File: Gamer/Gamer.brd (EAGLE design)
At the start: 168.9 x 63.5 mm, 44 parts, among them J1 HEADER-1X8, J2 HEADER-1X8, J3 HEADER-1X8, J4 HEADER-1X8, J5 HEADER-1X8, J6 HEADER-1X8, J7 HEADER-1X8, J8 HEADER-1X8, U1 MMA8653FCR1, U2 ATTINY48, U3 ULN2803AFWG, U4 ATTINY48, U5 ULN2803AFWG, U6 ATTINY48, U7 ULN2803AFWG, U8 ATTINY48, U9 ULN2803AFWG

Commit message: gamer - properly chained MISO/MOSI through LED matrices
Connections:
- new net 10/MISO: PROG4.4, U8.PB3
- new net MOSI2/MISO3: PROG2.4, PROG3.1, U4.PB3, U6.PB4
- new net MOSI3/MISO4: PROG3.4, PROG4.1, U6.PB3, U8.PB4
- net 9/MISO: no longer PROG2.1, PROG3.1, PROG4.1, U4.PB4, U6.PB4, U8.PB4
- net MOSI1/MISO2: now also PROG2.1, U4.PB4; no longer PROG2.4, PROG3.4, PROG4.4, U4.PB3, U6.PB3, U8.PB3
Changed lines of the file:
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@@
 <contactref element="P1" pad="21"/>
 <contactref element="U2" pad="PB4"/>
-<contactref element="U4" pad="PB4"/>
-<contactref element="U6" pad="PB4"/>
-<contactref element="U8" pad="PB4"/>
 <contactref element="PROG1" pad="1"/>
-<contactref element="PROG2" pad="1"/>
-<contactref element="PROG3" pad="1"/>
-<contactref element="PROG4" pad="1"/>
-<wire x1="133.35" y1="60.96" x2="143.51" y2="60.96" width="0" layer="19" extent="1-1"/>
-<wire x1="123.19" y1="60.96" x2="133.35" y2="60.96" width="0" layer="19" extent="1-1"/>
-<wire x1="113.03" y1="60.96" x2="123.19" y2="60.96" width="0" layer="19" extent="1-1"/>
-<wire x1="135.89" y1="44.45" x2="133.35" y2="60.96" width="0" layer="19" extent="1-1"/>
-<wire x1="95.51" y1="44.01" x2="113.03" y2="60.96" width="0" layer="19" extent="1-1"/>
-<wire x1="63.76" y1="44.01" x2="95.51" y2="44.01" width="0" layer="19" extent="1-1"/>
-<wire x1="95.51" y1="12.26" x2="95.51" y2="44.01" width="0" layer="19" extent="1-1"/>
-<wire x1="63.76" y1="12.26" x2="63.76" y2="44.01" width="0" layer="19" extent="1-1"/>
+<wire x1="113.03" y1="60.96" x2="135.89" y2="44.45" width="0" layer="19" extent="1-1"/>
+<wire x1="63.76" y1="44.01" x2="113.03" y2="60.96" width="0" layer="19" extent="1-1"/>
 </signal>
 <signal name="11/SCLK">
@@
 <contactref element="U2" pad="PB3"/>
 <contactref element="PROG1" pad="4"/>
-<contactref element="U4" pad="PB3"/>
-<contactref element="PROG2" pad="4"/>
-<contactref element="U6" pad="PB3"/>
-<contactref element="PROG3" pad="4"/>
-<contactref element="U8" pad="PB3"/>
-<contactref element="PROG4" pad="4"/>
-<wire x1="135.89" y1="58.42" x2="146.05" y2="58.42" width="0" layer="19" extent="1-1"/>
-<wire x1="125.73" y1="58.42" x2="135.89" y2="58.42" width="0" layer="19" extent="1-1"/>
-<wire x1="115.57" y1="58.42" x2="125.73" y2="58.42" width="0" layer="19" extent="1-1"/>
-<wire x1="94.71" y1="44.01" x2="115.57" y2="58.42" width="0" layer="19" extent="1-1"/>
-<wire x1="62.96" y1="44.01" x2="94.71" y2="44.01" width="0" layer="19" extent="1-1"/>
-<wire x1="94.71" y1="12.26" x2="94.71" y2="44.01" width="0" layer="19" extent="1-1"/>
-<wire x1="62.96" y1="12.26" x2="62.96" y2="44.01" width="0" layer="19" extent="1-1"/>
+<contactref element="U4" pad="PB4"/>
+<contactref element="PROG2" pad="1"/>
+<wire x1="115.57" y1="58.42" x2="123.19" y2="60.96" width="0" layer="19" extent="1-1"/>
+<wire x1="95.51" y1="44.01" x2="115.57" y2="58.42" width="0" layer="19" extent="1-1"/>
+<wire x1="62.96" y1="44.01" x2="95.51" y2="44.01" width="0" layer="19" extent="1-1"/>
 </signal>
 <signal name="M1_RESET">
@@
 <wire x1="92.31" y1="20.76" x2="101.6" y2="20.535" width="0" layer="19" extent="1-1"/>
 </signal>
+<signal name="MOSI2/MISO3">
+<contactref element="U4" pad="PB3"/>
+<contactref element="PROG2" pad="4"/>
+<contactref element="U6" pad="PB4"/>
+<contactref element="PROG3" pad="1"/>
+<wire x1="125.73" y1="58.42" x2="133.35" y2="60.96" width="0" layer="19" extent="1-1"/>
+<wire x1="94.71" y1="44.01" x2="125.73" y2="58.42" width="0" layer="19" extent="1-1"/>
+<wire x1="63.76" y1="12.26" x2="94.71" y2="44.01" width="0" layer="19" extent="1-1"/>
+</signal>
+<signal name="MOSI3/MISO4">
+<contactref element="U6" pad="PB3"/>
+<contactref element="U8" pad="PB4"/>
+<contactref element="PROG4" pad="1"/>
+<contactref element="PROG3" pad="4"/>
+<wire x1="135.89" y1="58.42" x2="143.51" y2="60.96" width="0" layer="19" extent="1-1"/>
+<wire x1="95.51" y1="12.26" x2="135.89" y2="58.42" width="0" layer="19" extent="1-1"/>
+<wire x1="62.96" y1="12.26" x2="95.51" y2="12.26" width="0" layer="19" extent="1-1"/>
+</signal>
+<signal name="10/MISO">
+<contactref element="U8" pad="PB3"/>
+<contactref element="PROG4" pad="4"/>
+<wire x1="94.71" y1="12.26" x2="146.05" y2="58.42" width="0" layer="19" extent="1-1"/>
+</signal>
 </signals>

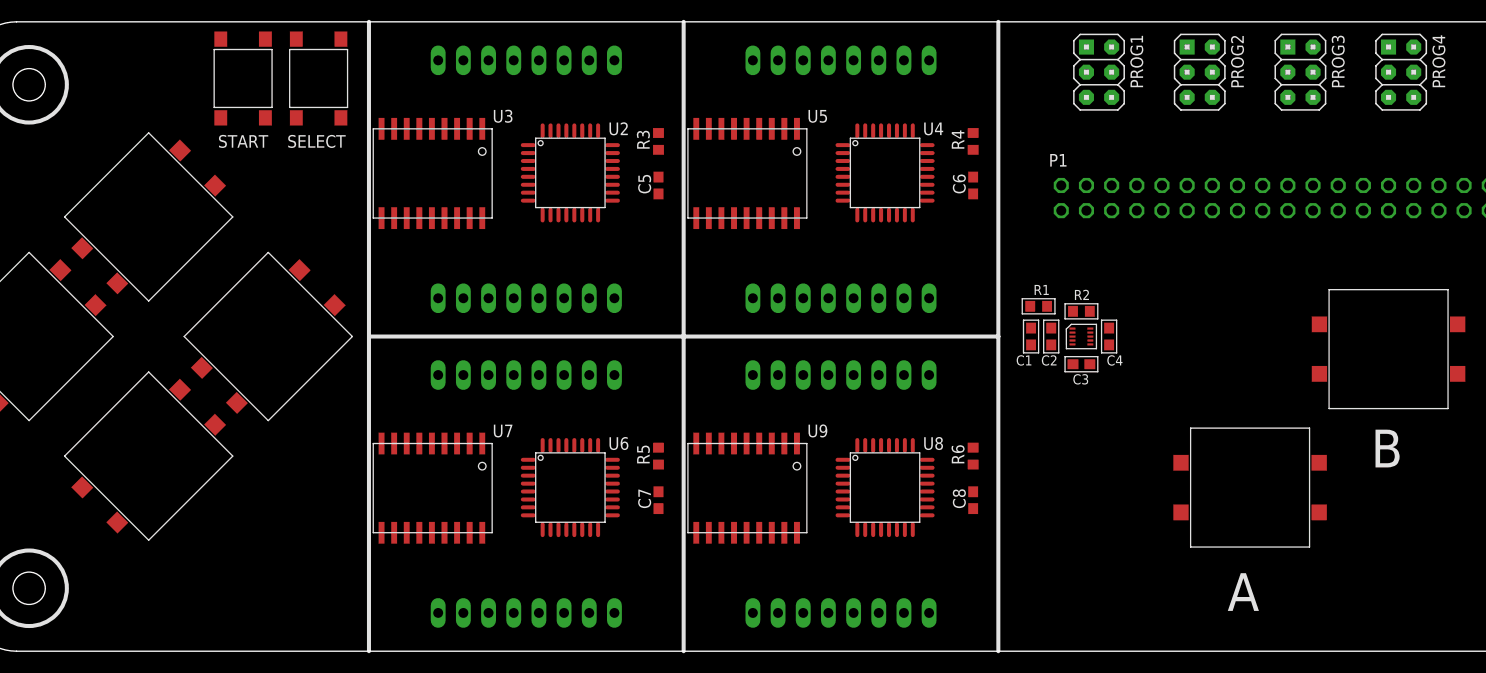
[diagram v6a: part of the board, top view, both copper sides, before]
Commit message: gamer - fully routed, first attempt
Will need to be rerouted, if middle mounting holes are added.
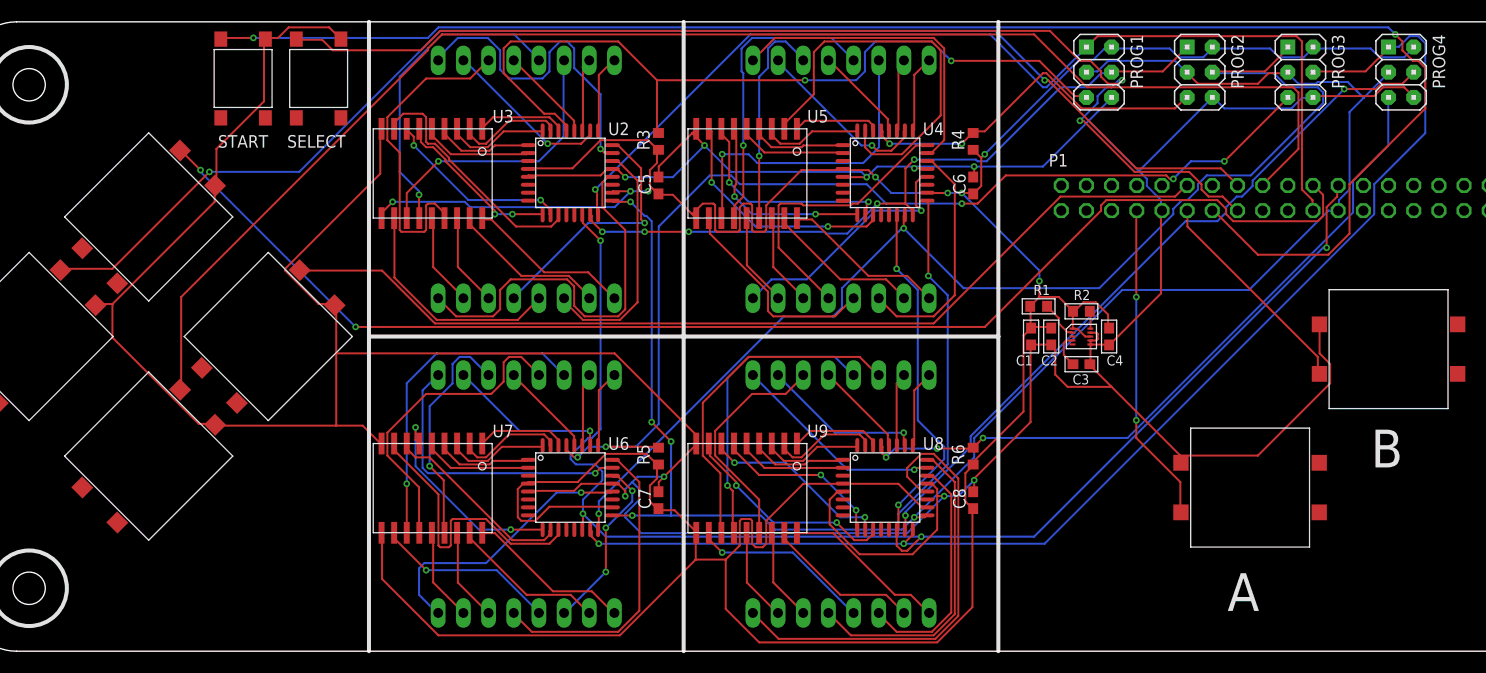
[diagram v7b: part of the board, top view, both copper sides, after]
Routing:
- net GND: track 0.00 -> 458.2 mm, vias 0 -> 9
- net VCC: track 0.00 -> 371.3 mm, vias 0 -> 8
- net 11/SCLK: track 0.00 -> 208.5 mm, vias 0 -> 6
- net 8/CE0: track 0.00 -> 172.9 mm, vias 0 -> 6
- net 27: track 0.00 -> 160.7 mm, vias 0 -> 2
- net 24: track 0.00 -> 146.5 mm
- net 23: track 0.00 -> 135.2 mm, vias 0 -> 2
- net 25: track 0.00 -> 133.4 mm, vias 0 -> 2
- net MOSI3/MISO4: track 0.00 -> 128.1 mm, vias 0 -> 2
- net MOSI2/MISO3: track 0.00 -> 122.6 mm, vias 0 -> 2
- net 22: track 0.00 -> 113.6 mm, vias 0 -> 2
- net M3_RESET: track 0.00 -> 108.2 mm, vias 0 -> 5
- net 9/MISO: track 0.00 -> 102.6 mm, vias 0 -> 1
- net 18: track 0.00 -> 97.5 mm
- net M1_RESET: track 0.00 -> 82.7 mm, vias 0 -> 2
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
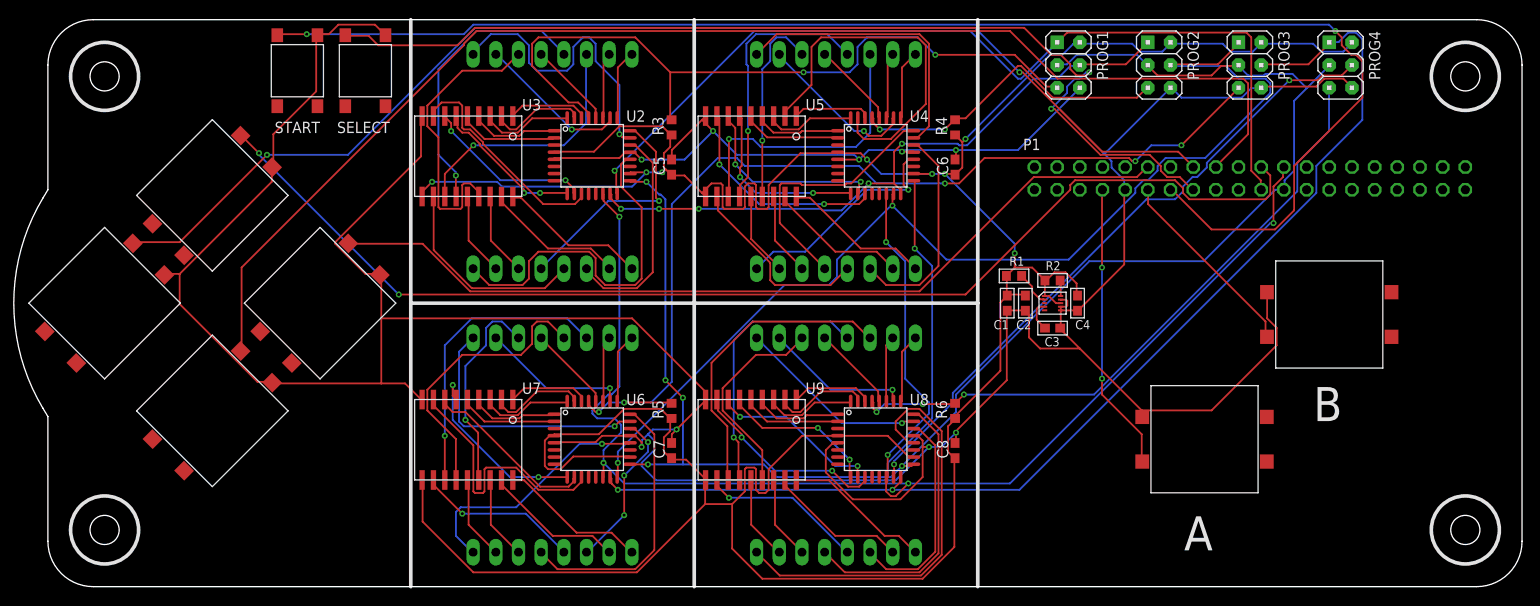
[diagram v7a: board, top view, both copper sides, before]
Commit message: gamer - partial routing, with ground plane and vias, and some hand routing
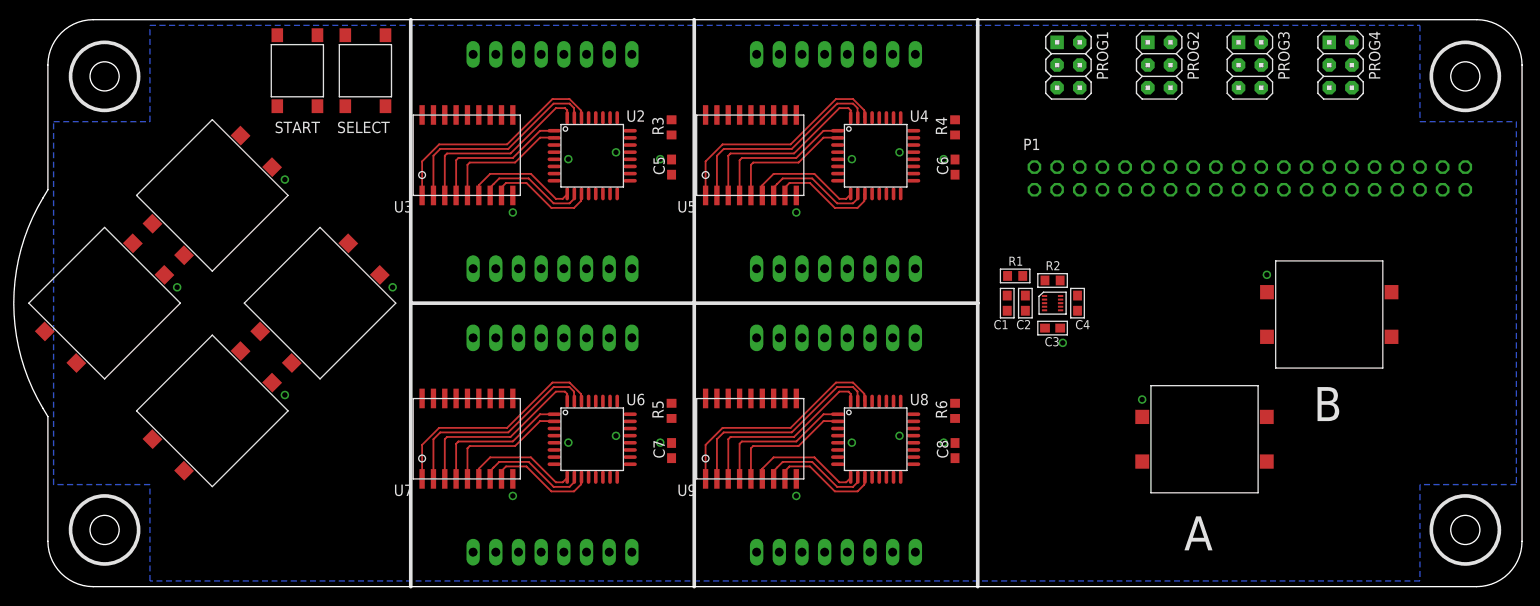
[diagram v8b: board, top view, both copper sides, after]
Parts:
- moved U3 13.5 mm to (41.9, 43.8), turned to 0 degrees
- moved U7 13.5 mm to (41.9, 12.1), turned to 0 degrees
- moved U5 13.5 mm to (73.7, 43.8), turned to 0 degrees
- moved U9 13.5 mm to (73.7, 12.1), turned to 0 degrees
- moved R1 0.13 mm to (108.3, 34.8)
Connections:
- net 3.3V_2 renamed 3V3_2
- removed net 3.3V_1: P1.1
- removed net GND: A.1, B.1, C1.2, C2.2, C3.2, C4.2, C5.2, C6.2, C7.2, C8.2, DOWN.4, LEFT.4, P1.9, PROG1.6, PROG2.6, PROG3.6, PROG4.6, RIGHT.4, SELECT.4, START.4, U1.6, U1.7, U1.9, U2.AGND, U2.GND, U3.GND, U4.AGND, U4.GND, U5.GND, U6.AGND, U6.GND, U7.GND, U8.AGND, U8.GND, U9.GND, UP.4
- removed net SCL: R1.1, U1.2
- removed net SDA: R2.1, U1.10
- removed net VCC: C1.1, C2.1, C4.1, C5.1, C6.1, C7.1, C8.1, PROG1.2, PROG2.2, PROG3.2, PROG4.2, R1.2, R2.2, R3.1, R4.1, R5.1, R6.1, U1.1, U1.8, U2.AVCC, U2.VCC, U3.COMMON, U4.AVCC, U4.VCC, U5.COMMON, U6.AVCC, U6.VCC, U7.COMMON, U8.AVCC, U8.VCC, U9.COMMON
- new net 3V3: C1.1, C2.1, C4.1, C5.1, C6.1, C7.1, C8.1, P1.1, PROG1.2, PROG2.2, PROG3.2, PROG4.2, R1.2, R2.2, R3.1, R4.1, R5.1, R6.1, U1.1, U1.8, U2.AVCC, U2.VCC, U3.COMMON, U4.AVCC, U4.VCC, U5.COMMON, U6.AVCC, U6.VCC, U7.COMMON, U8.AVCC, U8.VCC, U9.COMMON
- new net EEE: A.1, B.1, C1.2, C2.2, C3.2, C4.2, C5.2, C6.2, C7.2, C8.2, DOWN.4, LEFT.4, P1.9, PROG1.6, PROG2.6, PROG3.6, PROG4.6, RIGHT.4, SELECT.3, START.3, U1.6, U1.7, U1.9, U2.AGND, U2.GND, U3.GND, U4.AGND, U4.GND, U5.GND, U6.AGND, U6.GND, U7.GND, U8.AGND, U8.GND, U9.GND, UP.4
- new net N$1: START.4
- net 2/SDA: now also R2.1, U1.10
- net 3/SCL: now also R1.1, U1.2
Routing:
- net GND: track 458.2 -> 0.00 mm, vias 9 -> 0
- net VCC: track 371.3 -> 0.00 mm, vias 8 -> 0
- net 11/SCLK: track 208.5 -> 0.00 mm, vias 6 -> 0
- net 8/CE0: track 172.9 -> 0.00 mm, vias 6 -> 0
- net 27: track 160.7 -> 0.00 mm, vias 2 -> 0
- net 24: track 146.5 -> 0.00 mm
- net 23: track 135.2 -> 0.00 mm, vias 2 -> 0
- net 25: track 133.4 -> 0.00 mm, vias 2 -> 0
- net MOSI3/MISO4: track 128.1 -> 0.00 mm, vias 2 -> 0
- net MOSI2/MISO3: track 122.6 -> 0.00 mm, vias 2 -> 0
- net 22: track 113.6 -> 0.00 mm, vias 2 -> 0
- net M3_RESET: track 108.2 -> 0.00 mm, vias 5 -> 0
- net 9/MISO: track 102.6 -> 0.00 mm, vias 1 -> 0
- net 18: track 97.5 -> 0.00 mm
- net M1_RESET: track 82.7 -> 0.00 mm, vias 2 -> 0
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- added copper zone on layer 16, net EEE
